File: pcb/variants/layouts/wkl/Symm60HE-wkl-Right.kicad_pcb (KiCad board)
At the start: 2 copper layers, 145.9 x 104.7 mm, 170 parts

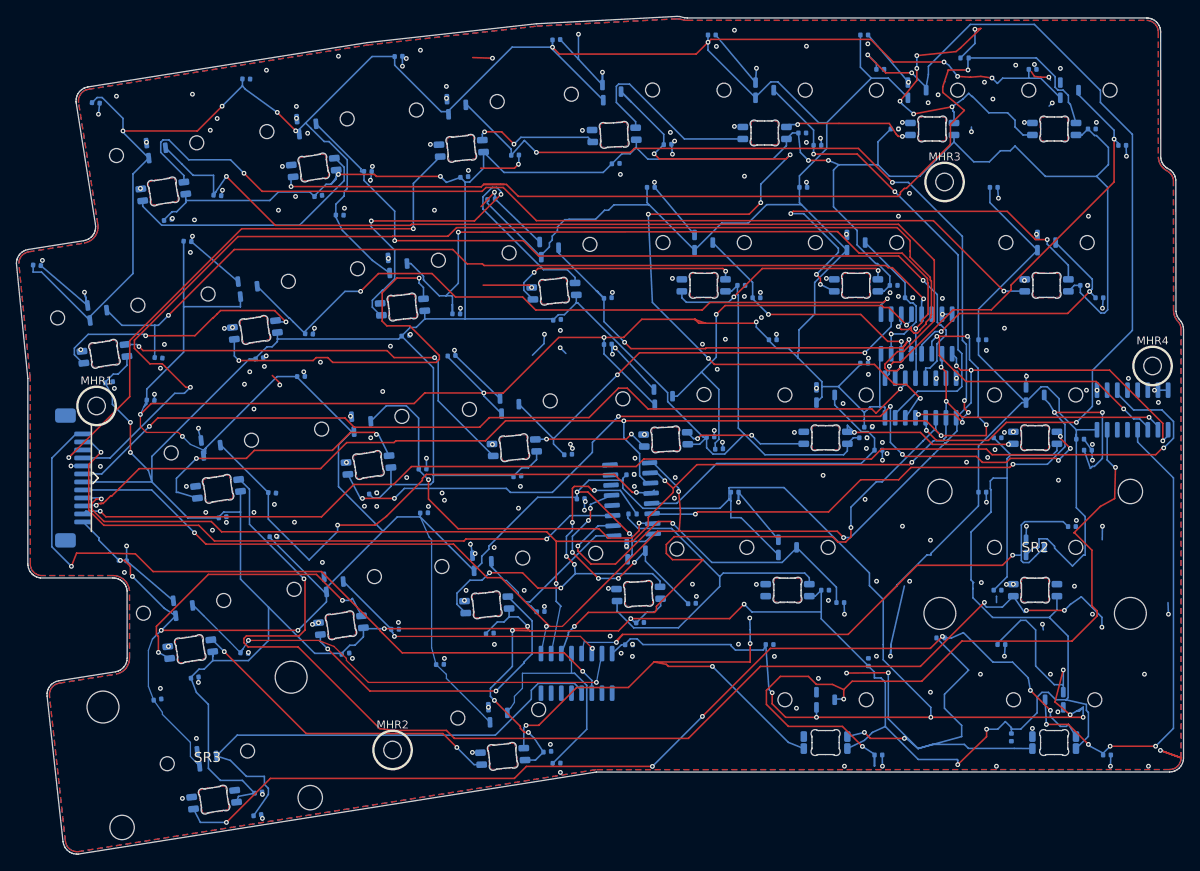
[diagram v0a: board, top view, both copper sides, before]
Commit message: Publish routed WKL PCBs and remove unrouted starters
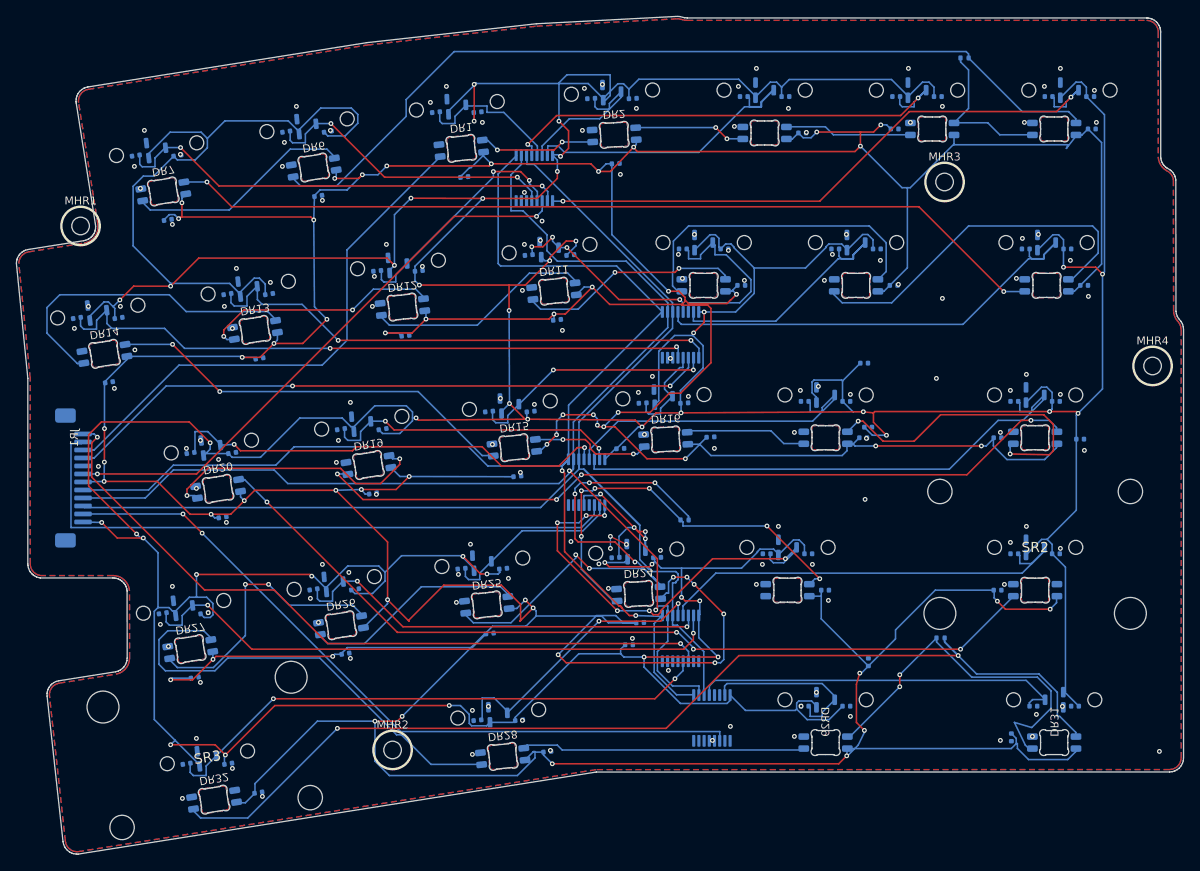
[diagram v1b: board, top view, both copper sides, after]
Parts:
- AMR1, AMR2, AMR3, AMR4, AMR5: footprint Symm60HE_Project:AM1_SOIC-16_3.9x9.9mm_P1.27mm -> Symm60HE_Project:AM1_TSSOP-16_4.4x5mm_P0.65mm
- RBPR24, RBPR31, RBPR5: footprint Symm60HE_Project:R3_R_0402_1005Metric -> Symm60HE_Project:R3_R_0402_1005Metric_DNP
- moved AMR5 65.2 mm to (243.9, 88.0), turned to 90 degrees
- moved AMR1 55.5 mm to (221.7, 20.5), turned to 90 degrees
- moved AMR2 29.5 mm to (240.0, 40.1), turned to 90 degrees
- moved MHR1 22.6 mm to (165.0, 26.5)
- moved AMR4 13.7 mm to (240.0, 78.0)
- moved CR31A 12.3 mm to (260.7, 86.5)
- moved CR8A 12.1 mm to (177.1, 17.7), turned to 9 degrees
- moved CR14A 12.1 mm to (188.6, 35.0), turned to 9 degrees
- moved CR20A 12.1 mm to (202.8, 51.9), turned to 9 degrees
- moved CR21A 12.1 mm to (183.9, 54.9), turned to 9 degrees
- moved CR28A 12.1 mm to (199.3, 71.9), turned to 9 degrees
- moved CR29A 12.1 mm to (180.5, 74.9), turned to 9 degrees
- moved CR15A 12.1 mm to (169.7, 38.0), turned to 9 degrees
- moved CR7A 12.1 mm to (195.9, 14.7), turned to 9 degrees
- moved CR6A 12.1 mm to (214.6, 12.3), turned to 6 degrees
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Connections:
- AMR3 pad 1: HE_R21 -> HE_R23
- AMR3 pad 2: HE_R23 -> HE_R21
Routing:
- net GND: track 208.1 -> 3.74 mm, vias 265 -> 150
- net VBUS: track 753.8 -> 881.7 mm, vias 15 -> 59
- net MUX_A0: track 254.2 -> 165.8 mm, vias 9 -> 0
- net HE_R02: track 105.1 -> 20.3 mm, vias 6 -> 0
- net HE_R01: track 102.4 -> 19.0 mm, vias 6 -> 0
- net +3V3A: track 1028.1 -> 951.9 mm, vias 26 -> 44
- net HE_R35: track 96.8 -> 21.9 mm, vias 3 -> 0
- net HE_R07: track 127.4 -> 57.6 mm
- net ADC_R2: track 148.9 -> 81.6 mm
- net HE_R08: track 93.8 -> 30.0 mm
- net HE_R06: track 101.9 -> 38.0 mm
- net ADC_R5: track 152.4 -> 92.1 mm
- net HE_R04: track 110.2 -> 60.2 mm, vias 4 -> 2
- net RGB_R_20: track 155.5 -> 108.5 mm, vias 5 -> 4
- net ADC_R1: track 111.7 -> 72.2 mm
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
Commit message: Publish 2026-10-05 production PCBs and firmware
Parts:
- moved AMR2 36.5 mm to (207.0, 24.5)
- moved AMR4 36.3 mm to (207.0, 63.0)
- moved MHR1 22.6 mm to (167.0, 49.0)
- moved AMR5 18.9 mm to (226.6, 80.4)
- moved AMR1 13.3 mm to (235.0, 21.0)
- moved AMR3 5.67 mm to (233.5, 60.7)
- moved CR31A 5.27 mm to (266.0, 86.5)
- moved CR19B 5.07 mm to (220.9, 48.2), turned to 6 degrees
- moved CR16A 5.04 mm to (245.5, 48.6)
- moved CRGBR2 4.52 mm to (228.5, 21.7)
- moved CRGBR14 3.95 mm to (172.5, 45.9), turned to -90 degrees
- moved CRGBR13 2.95 mm to (187.4, 46.0)
- moved CRGBR6 2.25 mm to (194.7, 25.0)
- moved CRGBR5 1.59 mm to (293.0, 14.4)
- moved CR8A 0.40 mm to (177.1, 18.1)
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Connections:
- AMR1 pad 1: HE_R05 -> HE_R12
- AMR1 pad 12: HE_R04 -> HE_R02
- AMR1 pad 13: HE_R01 -> HE_R03
- AMR1 pad 14: HE_R02 -> HE_R04
- AMR1 pad 15: HE_R03 -> HE_R05
- AMR1 pad 2: HE_R07 -> HE_R11
- AMR1 pad 4: HE_R08 -> HE_R10
- AMR1 pad 5: HE_R06 -> HE_R09
- AMR2 pad 1: HE_R13 -> GND
- AMR2 pad 12: HE_R12 -> HE_R07
- AMR2 pad 13: HE_R09 -> HE_R06
- AMR2 pad 14: HE_R10 -> HE_R01
- AMR2 pad 15: HE_R11 -> GND
- AMR2 pad 2: HE_R15 -> HE_R08
- AMR2 pad 4: HE_R16 -> HE_R13
- AMR3 pad 1: HE_R23 -> HE_R25
- AMR3 pad 12: HE_R20 -> HE_R15
- AMR3 pad 13: HE_R17 -> HE_R16
- AMR3 pad 14: HE_R18 -> HE_R17
- AMR3 pad 15: HE_R19 -> HE_R18
- AMR3 pad 2: HE_R21 -> HE_R23
- AMR3 pad 4: HE_R24 -> HE_R22
- AMR3 pad 5: HE_R22 -> HE_R21
- AMR4 pad 1: HE_R29 -> GND
- AMR4 pad 12: HE_R28 -> HE_R20
- AMR4 pad 13: HE_R25 -> HE_R19
- AMR4 pad 14: HE_R26 -> GND
- AMR4 pad 15: HE_R27 -> GND
- AMR4 pad 2: HE_R31 -> GND
- AMR4 pad 4: HE_R32 -> HE_R26
- AMR4 pad 5: HE_R30 -> HE_R27
- AMR5 pad 1: GND -> HE_R36
- AMR5 pad 12: HE_R36 -> GND
- AMR5 pad 13: HE_R33 -> GND
- AMR5 pad 14: HE_R34 -> GND
- AMR5 pad 15: HE_R35 -> GND
- AMR5 pad 2: GND -> HE_R35
- AMR5 pad 4: GND -> HE_R28
- AMR5 pad 5: GND -> HE_R32
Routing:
- net +3V3A: track 951.9 -> 1181.4 mm, vias 44 -> 83
- net VBUS: track 881.7 -> 1004.0 mm, vias 59 -> 62
- net RGB_R_05: track 110.9 -> 204.6 mm, vias 0 -> 2
- net RGB_R_07: track 110.8 -> 181.7 mm, vias 2 -> 0
- net ADC_R3: track 79.4 -> 135.8 mm, vias 0 -> 4
- net MUX_A2: track 166.6 -> 214.5 mm, vias 2 -> 10
- net MUX_A1: track 164.6 -> 211.7 mm, vias 2 -> 10
- net MUX_A0: track 165.8 -> 210.3 mm, vias 0 -> 10
- net HE_R13: track 67.2 -> 30.3 mm, vias 2 -> 0
- net HE_R27: track 74.9 -> 38.3 mm, vias 2 -> 0
- net HE_R35: track 21.9 -> 57.8 mm
- net ADC_R1: track 72.2 -> 107.8 mm, vias 2 -> 0
- net HE_R26: track 53.3 -> 18.8 mm, vias 2 -> 0
- net HE_R14: track 82.1 -> 49.7 mm, vias 2 -> 0
- net ADC_R4: track 92.1 -> 62.9 mm, vias 2 -> 4
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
